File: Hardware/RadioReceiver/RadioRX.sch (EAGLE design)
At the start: 49 parts, among them IC1 7805TV, Q1 BSS123, Q10 BSS123, Q11 BSS123, Q12 BSS123, Q13 BSS123, Q14 BSS123, Q2 BSS123, Q3 BSS84, Q4 BSS84, Q5 BSS84, Q6 BSS84, Q7 BSS123, Q8 BSS123, Q9 BSS123

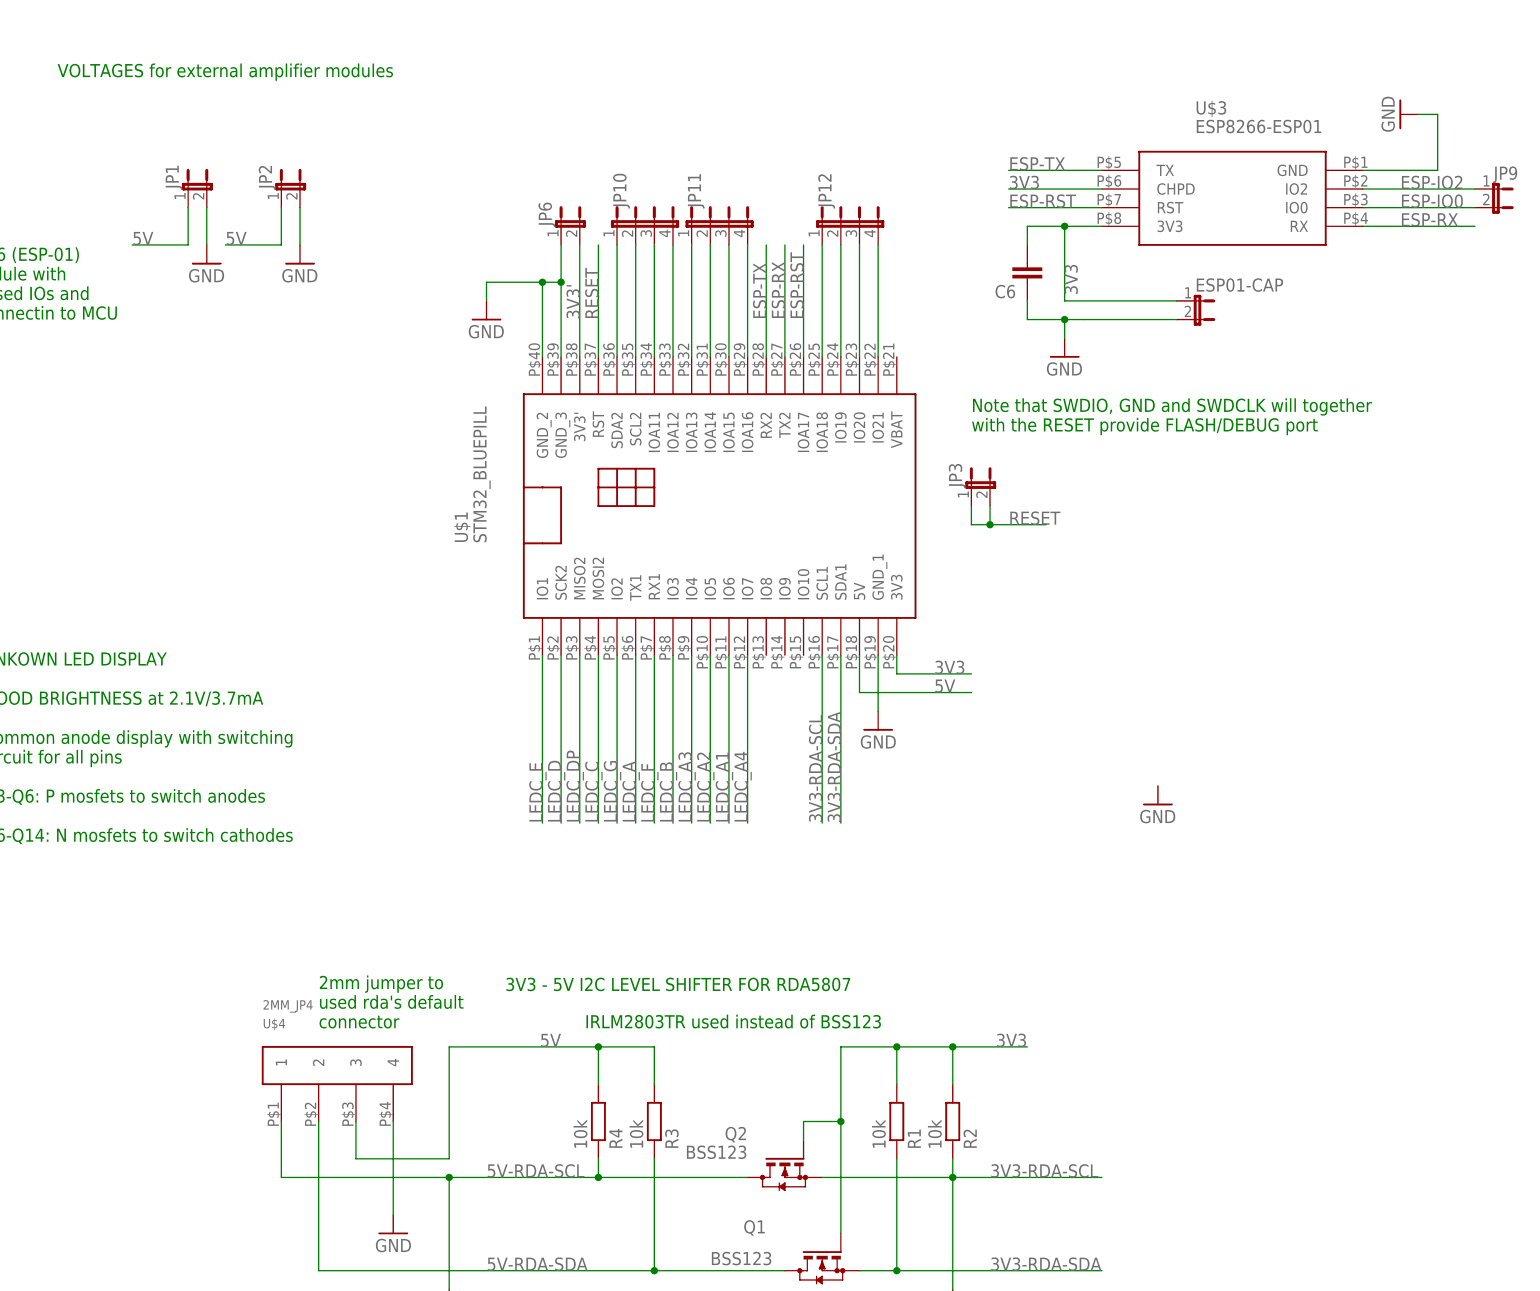
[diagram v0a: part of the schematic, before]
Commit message: Cleaned HW, prepared for NCODER, time (slows 1minute/hours)
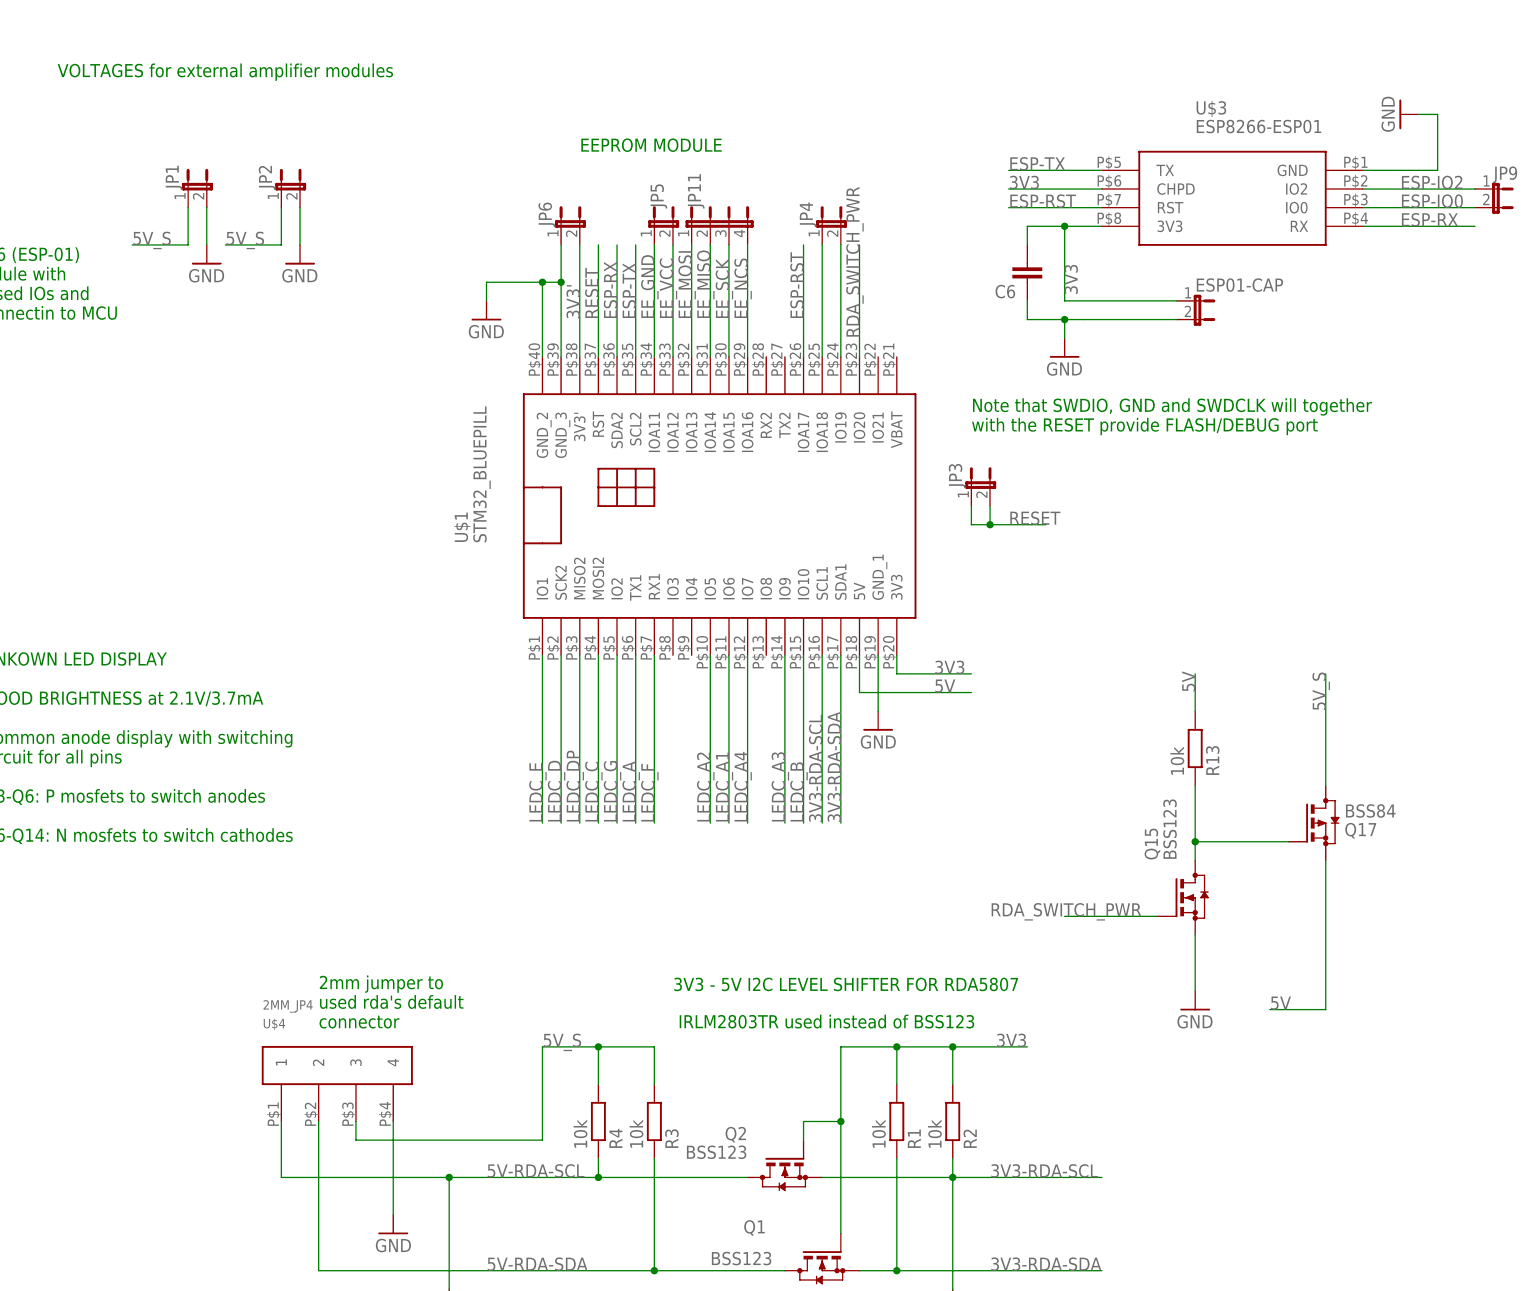
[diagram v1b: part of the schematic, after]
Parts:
- removed JP10, JP12: (no value), jumper:JP4E
- added JP4, JP5: (no value), jumper:JP1E
- added Q15: BSS123, transistor-small-signal:BSS123
- added Q17: BSS84, transistor-small-signal:BSS84
- added R13: 10k, rcl:R-EU_R0805
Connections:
- net N$10 renamed EE_NCS
- net N$7 renamed EE_MOSI
- net N$8 renamed EE_MISO
- net N$9 renamed EE_SCK
- removed net N$13: JP12.3, U$1.IO20
- removed net N$14: JP12.4, U$1.IO21
- removed net N$3: JP10.1, U$1.SDA2
- removed net N$4: JP10.2, U$1.SCL2
- removed net N$5: JP10.3, U$1.IOA11
- removed net N$6: JP10.4, U$1.IOA12
- new net 5V_S: JP1.1, JP2.1, Q17.D, R3.2, R4.2, U$4.3
- new net EE_GND: JP5.1, U$1.IOA11
- new net EE_VCC: JP5.2, U$1.IOA12
- new net N$15: Q15.D, Q17.G, R13.1
- new net RDA_SWITCH_PWR: Q15.G, U$1.IO20
- net 5V: now also Q17.S, R13.2; no longer JP1.1, JP2.1, R3.2, R4.2, U$4.3
- net ESP-RX: now also U$1.SDA2; no longer U$1.TX2
- net ESP-TX: now also U$1.SCL2; no longer U$1.RX2
- net GND: now also Q15.S
- net LEDC_A3: now also U$1.IO9; no longer U$1.IO4
- net LEDC_B: now also U$1.IO10; no longer U$1.IO3
- net N$11: now also JP4.1; no longer JP12.1
- net N$12: now also JP4.2; no longer JP12.2
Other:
- note added: "EEPROM MODULE"

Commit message: Almost final state, just a 32.768 XTAL misses to be soldered
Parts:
- removed DC_CONN: DC_CONN, VladimirSustek:DC_CONN
- removed IC1: 7805TV, linear:7805TV
- removed JP11: (no value), jumper:JP4E
- removed JP4, JP5, JP7, JP8: (no value), jumper:JP1E
- added C7, C8: 12p, rcl:C-EUC0603
- added EEPROM_0_1, IN_DC, I_MEAS, XTAL: (no value), jumper:JP1E
- added EEPROM_2_5: (no value), jumper:JP4E
- added IN_DC_JACK: DC_CONN, VladimirSustek:DC_CONN
- added LDO: 7805TV, linear:7805TV
- C1, C2: value (none) -> DNI 100p
- C3, C5, C6: value (none) -> 100n
- C4: value (none) -> 10n
- R10, R11, R12, R5, R6, R7, R8, R9: value (none) -> 220R
- renumbered ESP01-CAP to ESP01-CAP,100UF, JP1 to VCC_AUDIO_1, JP2 to VCC_AUDIO_0, JP3 to RST, JP6 to D_VCC, JP9 to ESP_GPIO, U$1 to MCU_MODULE, U$2 to DISPLAY, U$3 to WIFI, U$4 to I2C_3V3_5V
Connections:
- removed net N$11: JP4.1, MCU_MODULE.IOA18
- removed net N$12: JP4.2, MCU_MODULE.IO19
- new net GREEN_LED: MCU_MODULE.IO21
- new net N$3: C8.2, MCU_MODULE.IO20, XTAL.2
- new net N$4: C7.2, MCU_MODULE.IO19, XTAL.1
- new net NCODER_BTN: MCU_MODULE.RX2
- new net NCODER_CLK: MCU_MODULE.IO8
- new net NCODER_IN: MCU_MODULE.TX2
- new net USB_DM: MCU_MODULE.IO3
- new net USB_DP: MCU_MODULE.IO4
- net 5V: now also LDO.VO; no longer IC1.VO
- net EE_GND: now also EEPROM_0_1.1; no longer JP5.1
- net EE_MISO: now also EEPROM_2_5.2; no longer JP11.2
- net EE_MOSI: now also EEPROM_2_5.1; no longer JP11.1
- net EE_NCS: now also EEPROM_2_5.4; no longer JP11.4
- net EE_SCK: now also EEPROM_2_5.3; no longer JP11.3
- net EE_VCC: now also EEPROM_0_1.2; no longer JP5.2
- net GND: now also C7.1, C8.1, IN_DC.1, IN_DC_JACK.GND, IN_DC_JACK.GND', LDO.GND; no longer DC_CONN.GND, DC_CONN.GND', IC1.GND, JP8.1
- net LEDC_B: now also Q12.G; no longer Q11.G
- net LEDC_C: now also Q10.G; no longer Q9.G
- net LEDC_D: now also Q8.G; no longer Q7.G
- net LEDC_DP: now also Q9.G; no longer Q8.G
- net LEDC_E: now also Q7.G; no longer Q13.G
- net LEDC_F: now also Q13.G; no longer Q12.G
- net LEDC_G: now also Q11.G; no longer Q10.G
- net N$1: now also I_MEAS.2, LDO.VI; no longer IC1.VI, JP7.2
- net N$18: now also Q7.D; no longer Q13.D
- net N$19: now also Q8.D; no longer Q7.D
- net N$2: now also IN_DC.2, IN_DC_JACK.BUS, I_MEAS.1; no longer DC_CONN.BUS, JP7.1, JP8.2
- net N$20: now also Q9.D; no longer Q8.D
- net N$21: now also Q10.D; no longer Q9.D
- net N$22: now also Q11.D; no longer Q10.D
- net N$23: now also Q12.D; no longer Q11.D
- net N$24: now also Q13.D; no longer Q12.D
- net RDA_SWITCH_PWR: now also MCU_MODULE.IOA18; no longer MCU_MODULE.IO20
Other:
- note added: "N-FET and P-FET cascade needed as the RDA_SWITCH_PWR operating at levels are 0V and 3V3 and the DRAIN voltage of the P-FET Q17 is 5V, just the 3V3 GATE voltage would not close the P-FET (5V-3.3V = 1.7V > V_GATE_TR). Cascade ensures the Q17 GATE is controlled using 0V and 5V levels"
- note added: "NEVER USE ID_DC_JACK TOGETHER WITH BLUEPILL's USB, THERE IS NO PROTECTION DIODE AND 7805 WILL TRY TO FEED CURRENT INTO YOUR USB EITHER USB POWERED OR IN_DC_JACK"
- note added: "This circuitry is optional as the BLUEPILL has its own USB power supply and as the 7805 is not the most efficient way When 7805 used, please use big enough alu-radiator that you dont cause a fire :-)"
- note added: "UNKOWN LED DISPLAY IF REUSING SCHEMATIC PLEASE CHECK WHETHER YOUR LED FITS INTO THE PINOUT OF THIS DISPLAY GOOD BRIGHTNESS at 2.1V/3.7mA Common anode display with switching circuit for all pins Q3-Q6: P mosfets to switch anodes Q6-Q14: N mosfets to switch cathodes"
- note removed: "EEPROM MODULE"
- note removed: "UNKOWN LED DISPLAY GOOD BRIGHTNESS at 2.1V/3.7mA Common anode display with switching circuit for all pins Q3-Q6: P mosfets to switch anodes Q6-Q14: N mosfets to switch cathodes"
- moved on the sheet: C3, C4, C5, Q10, Q11, Q12, Q13, Q7, Q8, Q9
